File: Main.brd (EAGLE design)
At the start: 103.8 x 80 mm, 55 parts, among them IC1 LM75A, IC2 ADUM1400, IC3 74LS14N, IC4 MCP2300X/P, Q1 IRF9530, U1 L298, U2 LM 1084 IT5,0, U3 LM 1084 IT3,3, U4 L298, X1 Motors, X3 Battery, X4 Ultra Sonics (5V), X5 ITG-3200, X6 PIRs (5V)

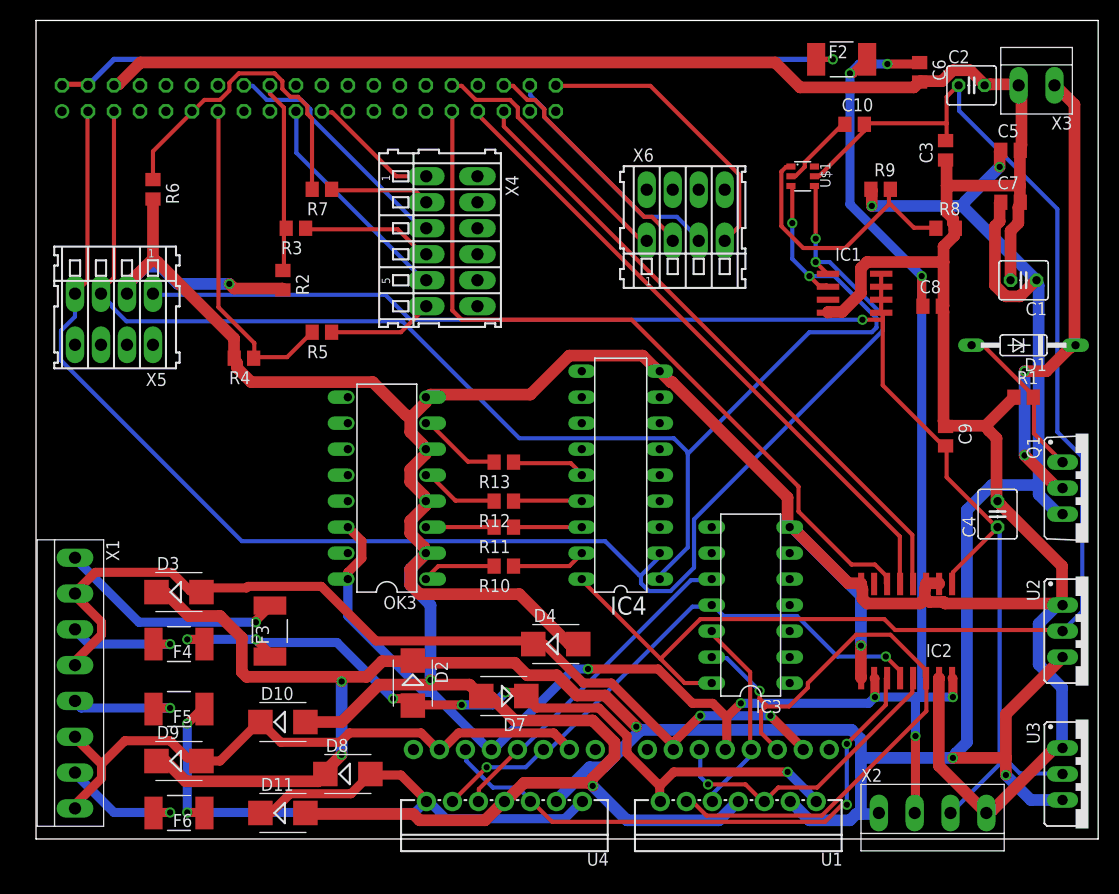
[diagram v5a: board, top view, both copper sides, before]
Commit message: placed Cs closer to corresponding parts
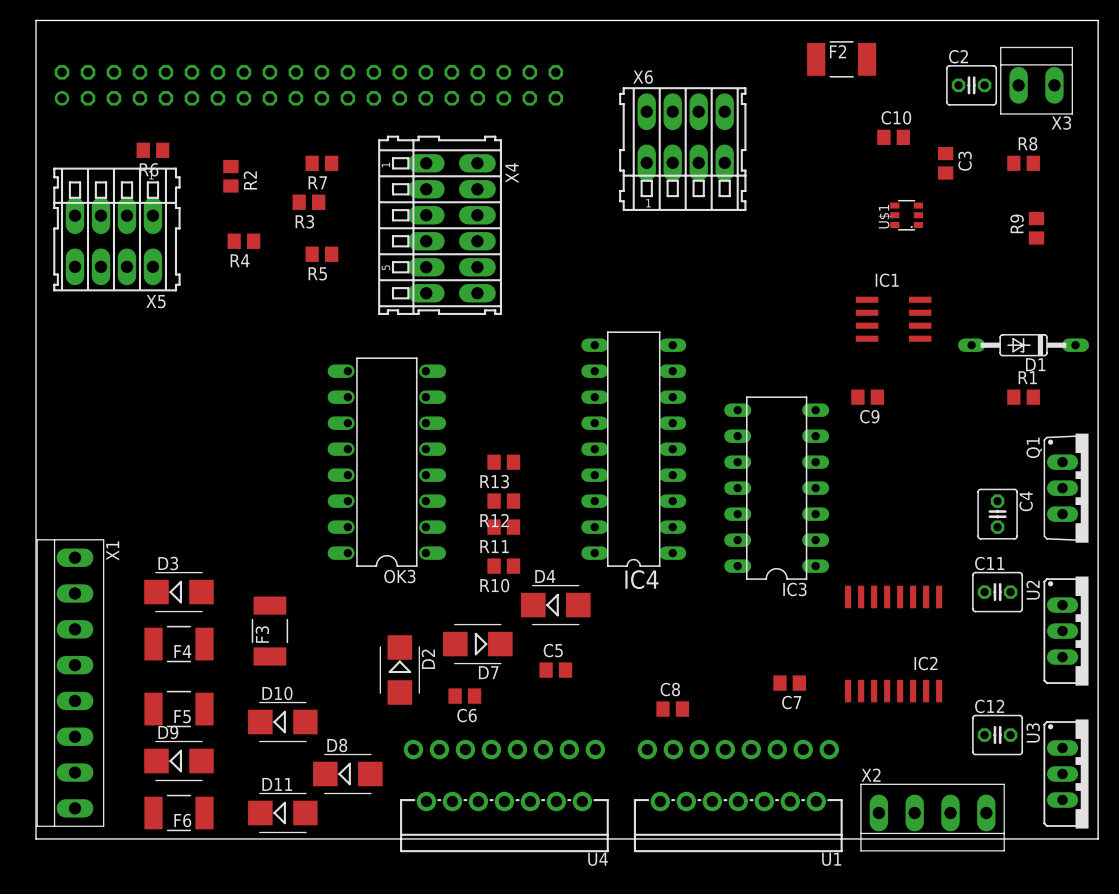
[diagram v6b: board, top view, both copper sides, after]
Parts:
- removed C1: 10uF Tant., rcl:C025-040X050
- added C11, C12: 10uF Tant., rcl:C025-040X050
- moved C6 75.4 mm to (41.9, 14.0), turned to 180 degrees
- moved C5 67.5 mm to (50.8, 16.5)
- moved C7 51.7 mm to (73.7, 15.2), turned to 180 degrees
- moved C8 46.9 mm to (62.2, 12.7)
- moved R9 15.7 mm to (97.8, 59.7), turned to 90 degrees
- moved IC3 11.7 mm to (72.4, 34.3)
- moved R4 11.4 mm to (20.3, 58.4)
- moved R2 11.4 mm to (19.1, 64.8)
- moved U$1 10.9 mm to (85.1, 61.0), turned to 90 degrees
- moved R8 9.92 mm to (96.5, 66.0)
- moved C9 8.52 mm to (81.3, 43.2), turned to 180 degrees
- moved X5 7.62 mm to (7.62, 58.4)
- moved R5 7.62 mm to (27.9, 57.1)
- moved X6 7.62 mm to (63.5, 68.6)
- moved D7 5.68 mm to (43.2, 19.1)
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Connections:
- net +12V: now also C11.1, C12.1; no longer C1.1
- net GND: now also C11.2, C12.2; no longer C1.2
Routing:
- net GND: track 529.6 -> 0.00 mm, vias 4 -> 0
- net +12V: track 266.7 -> 0.00 mm, vias 7 -> 0
- net +5V: track 175.3 -> 0.00 mm, vias 8 -> 0
- net SDA1: track 151.2 -> 0.00 mm, vias 2 -> 0
- net +3.3V: track 146.2 -> 0.00 mm, vias 1 -> 0
- net SCL1: track 140.3 -> 0.00 mm, vias 2 -> 0
- net VCC: track 138.9 -> 0.00 mm
- net ML_OUT_B: track 92.3 -> 0.00 mm, vias 2 -> 0
- net N$5: track 78.1 -> 0.00 mm, vias 1 -> 0
- net ML_OUT_A: track 77.0 -> 0.00 mm, vias 6 -> 0
- net MR_SPEED_: track 74.9 -> 0.00 mm
- net MR_OUT_A: track 72.1 -> 0.00 mm, vias 2 -> 0
- net ML_DIR: track 65.4 -> 0.00 mm, vias 1 -> 0
- net MR_DIR_: track 63.3 -> 0.00 mm
- net ML_SPEED_: track 62.8 -> 0.00 mm
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
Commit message: cleanup and notes
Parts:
- X5: value ITG-3200 -> ITG-3200 (3.3V); device con-wago:233-504 -> con-wago:233-502
- moved IC4 9.67 mm to (62.2, 29.2)
- moved C9 5.24 mm to (86.4, 44.5)
- moved IC3 3.59 mm to (74.9, 36.8)
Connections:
- net +3.3V: no longer X5.B1
- net GND: no longer X5.B2
- net SCL1: now also X5.B1; no longer X5.B3
- net SDA1: now also X5.B2; no longer X5.B4
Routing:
- net GND: track 0.00 -> 537.0 mm, vias 0 -> 7
- net +12V: track 0.00 -> 249.0 mm, vias 0 -> 8
- net +5V: track 0.00 -> 179.1 mm, vias 0 -> 5
- net SCL1: track 0.00 -> 154.2 mm, vias 0 -> 4
- net SDA1: track 0.00 -> 144.9 mm, vias 0 -> 3
- net VCC: track 0.00 -> 125.6 mm
- net MR_DIR: track 0.00 -> 99.9 mm, vias 0 -> 2
- net ML_OUT_A: track 0.00 -> 92.4 mm, vias 0 -> 7
- net ML_OUT_B: track 0.00 -> 90.0 mm, vias 0 -> 4
- net ML_SPEED_: track 0.00 -> 82.4 mm
- net N$5: track 0.00 -> 79.2 mm, vias 0 -> 1
- net MR_SPEED: track 0.00 -> 71.2 mm, vias 0 -> 2
- net MR_DIR_: track 0.00 -> 67.9 mm
- net MR_SPEED_: track 0.00 -> 67.5 mm
- net +3.3V: track 0.00 -> 67.4 mm
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
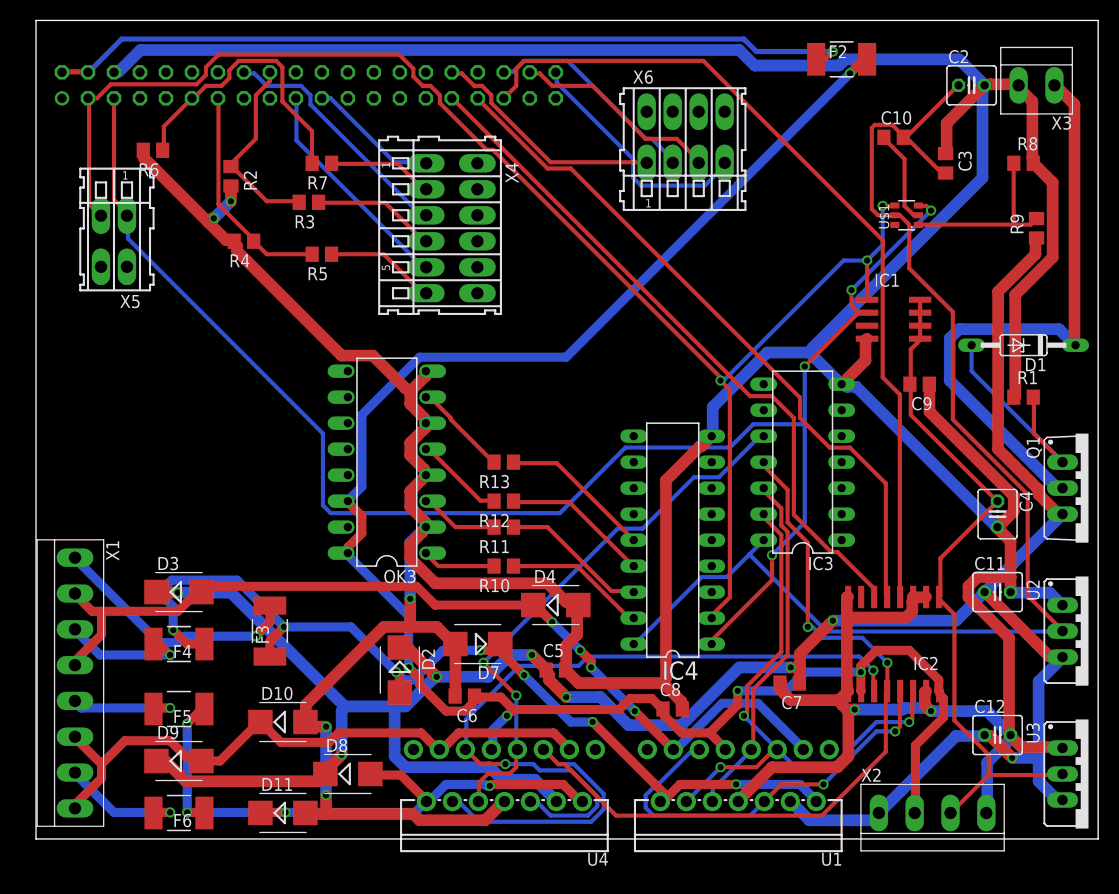
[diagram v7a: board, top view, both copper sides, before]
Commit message: more output switches
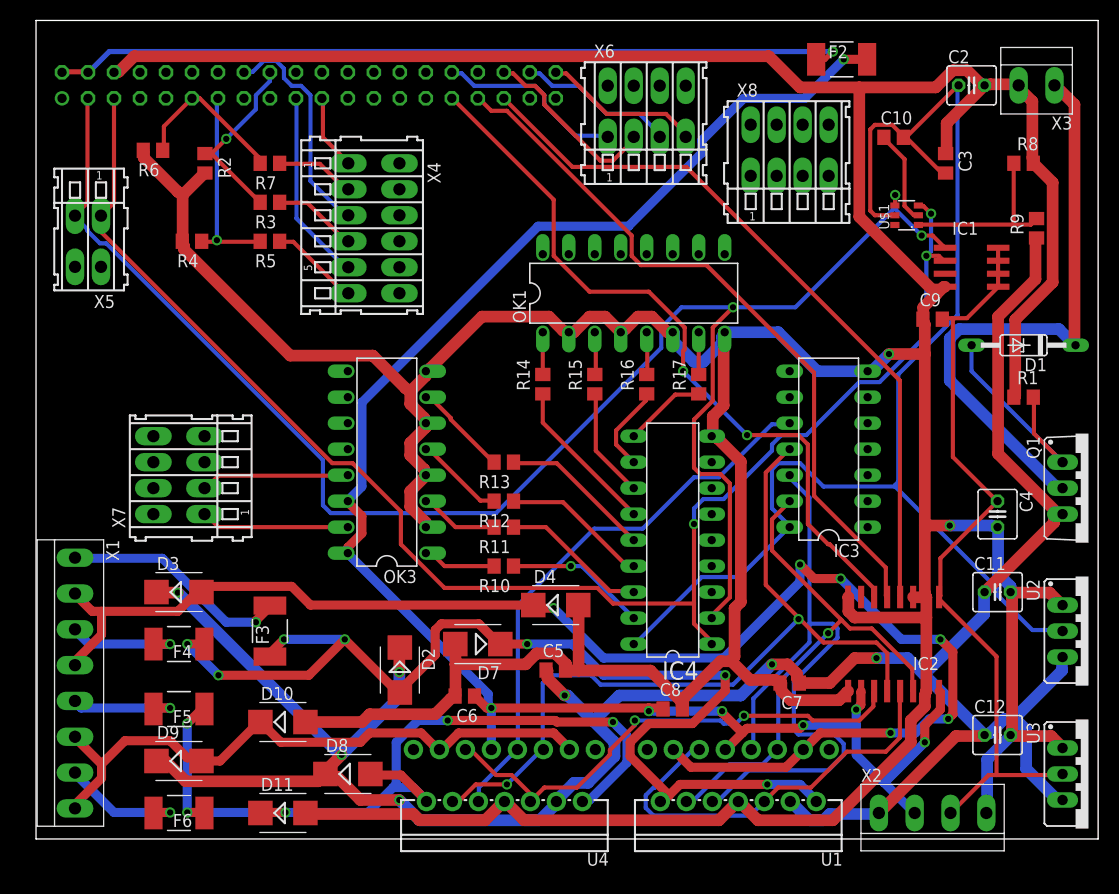
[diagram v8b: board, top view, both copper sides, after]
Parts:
- added OK1: PC847, optocoupler:DIL16
- added R14, R15, R16, R17: 120, resistor:R0805
- added X7, X8: (no value), con-wago:233-504
- moved IC1 9.16 mm to (91.4, 55.9)
- moved X4 7.62 mm to (33.0, 59.7)
- moved C9 6.48 mm to (87.6, 50.8), turned to 0 degrees
- moved R5 5.24 mm to (22.9, 58.4)
- moved R7 5.08 mm to (22.9, 66.0)
- moved R4 5.08 mm to (15.2, 58.4)
- moved X6 4.58 mm to (59.7, 71.1)
- moved R3 3.81 mm to (22.9, 62.2)
- moved R2 2.84 mm to (16.5, 66.0)
- moved IC3 2.84 mm to (77.5, 38.1)
- moved X5 2.54 mm to (5.08, 58.4)
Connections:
- new net DUBI: X7.B4
- new net N$1: OK1.1, R14.2
- new net N$12: OK1.7, R17.2
- new net N$27: X8.B1
- new net N$28: X8.B2
- new net N$29: X8.B3
- new net N$31: X8.B4
- new net N$38: OK3.12
- new net N$39: OK3.11
- new net N$43: OK3.10
- new net N$44: OK3.9
- new net N$45: OK1.16
- new net N$46: OK1.15
- new net N$47: OK1.14
- new net N$48: OK1.13
- new net N$49: OK1.12
- new net N$50: OK1.11
- new net N$51: OK1.10
- new net N$52: OK1.9
- new net N$6: OK1.3, R15.2
- new net N$8: OK1.5, R16.2
- new net SCHUBI: X7.B3
- net CAM_SERVO_AZI: now also X7.B1
- net CAM_SERVO_ELE: now also X7.B2
- net GND: now also OK1.2, OK1.4, OK1.6, OK1.8
- net GP0: now also R17.1
- net GP1: now also R16.1
- net GP2: now also R15.1
- net GP3: now also R14.1
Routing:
- net ML_OUT_B: track 90.0 -> 141.4 mm, vias 4 -> 6
- net ML_B: track 34.7 -> 65.9 mm
- net MR_SPEED: track 71.2 -> 49.2 mm
- net MR_OUT_A: track 62.4 -> 84.0 mm, vias 4 -> 5
- net MR_DIR: track 99.9 -> 78.7 mm
- net SDA1: track 144.9 -> 164.6 mm
- net GND: track 537.0 -> 555.4 mm, vias 7 -> 2
- net ML_OUT_A: track 92.4 -> 110.1 mm
- net GP3: track 0.00 -> 15.4 mm
- net CAM_SERVO_ELE: track 0.00 -> 14.6 mm
- net CAM_SERVO_AZI: track 0.00 -> 14.5 mm
- net USM_A_ECHO: track 27.9 -> 15.9 mm
- net ML_SPEED_: track 82.4 -> 71.3 mm
- net GP2: track 0.00 -> 10.8 mm
- net GP1: track 0.00 -> 8.64 mm
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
